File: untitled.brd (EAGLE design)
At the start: 41.6 x 28.6 mm, 21 parts, among them IC1 ACS758LCB-050B-PFF-T

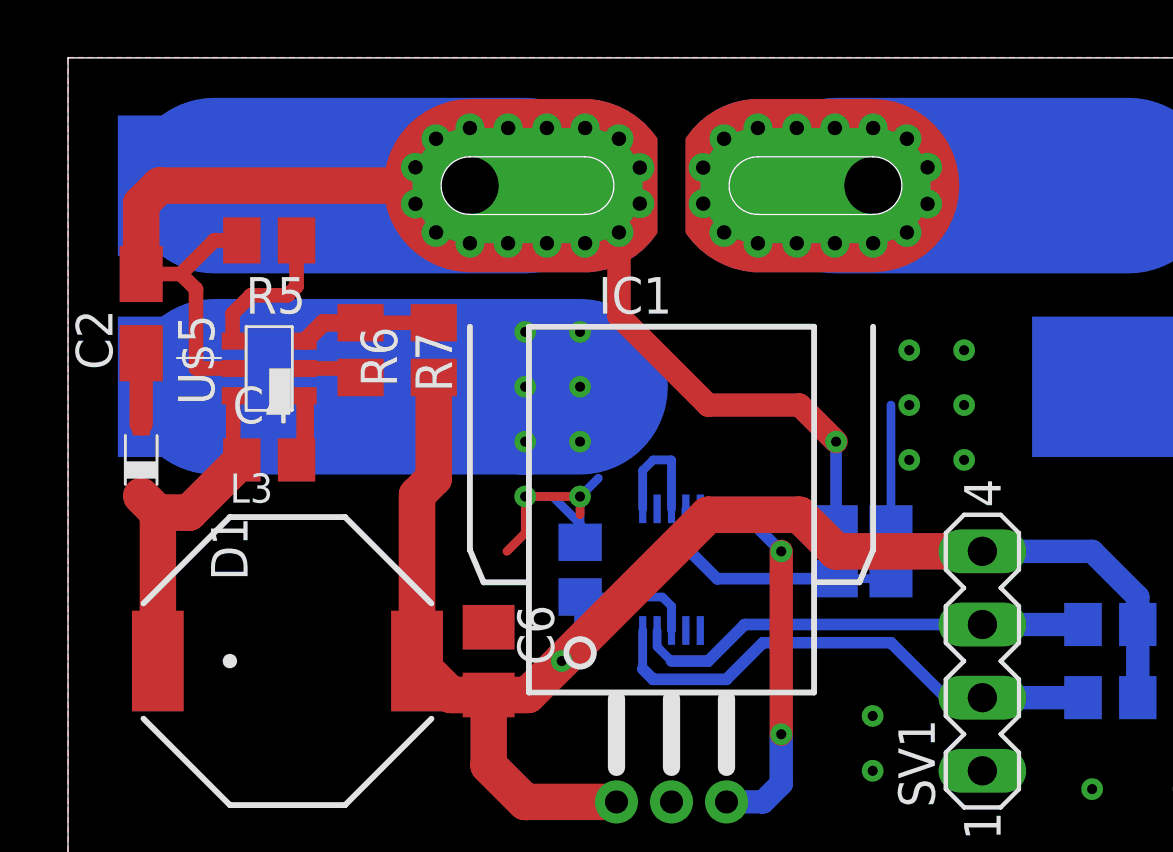
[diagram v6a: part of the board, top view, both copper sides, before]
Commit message: Update board layout based on bought components
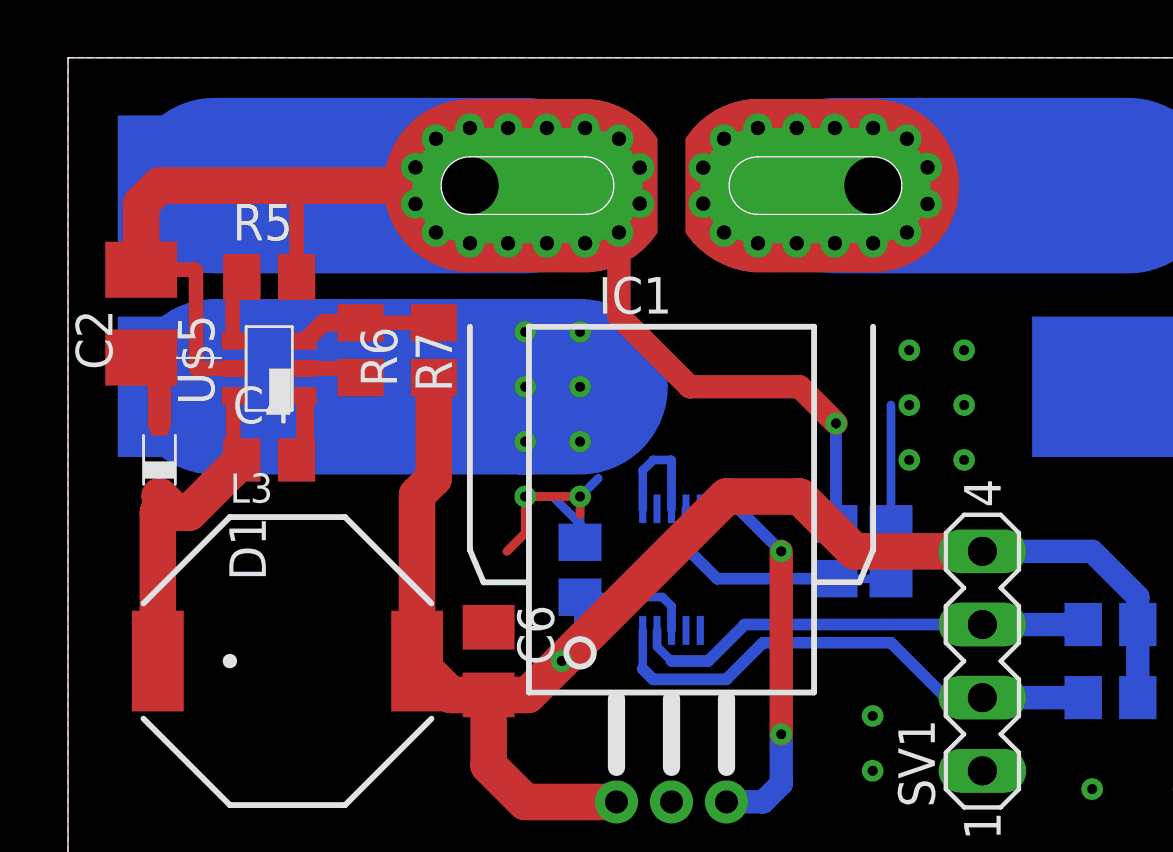
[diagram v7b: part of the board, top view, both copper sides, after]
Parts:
- C2: device rcl:A/3216-18R -> rcl:B/3528-21R
- moved R5 1.27 mm to (23.5, 36.2), turned to 0 degrees
- moved D1 0.63 mm to (19.7, 29.8)
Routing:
- net N$3: track 5.19 -> 2.55 mm
- net N$4: track 56.7 -> 58.1 mm
- net VCC: track 57.2 -> 57.7 mm
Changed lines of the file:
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@@
 <drawing>
 <settings>
-<setting alwaysvectorfont="yes"/>
+<setting alwaysvectorfont="no"/>
 <setting verticaltext="up"/>
 </settings>
@@
 <layer number="40" name="bKeepout" color="1" fill="11" visible="no" active="yes"/>
 <layer number="41" name="tRestrict" color="4" fill="10" visible="no" active="yes"/>
-<layer number="42" name="bRestrict" color="1" fill="10" visible="yes" active="yes"/>
+<layer number="42" name="bRestrict" color="1" fill="10" visible="no" active="yes"/>
 <layer number="43" name="vRestrict" color="2" fill="10" visible="no" active="yes"/>
 <layer number="44" name="Drills" color="7" fill="1" visible="no" active="yes"/>
-<layer number="45" name="Holes" color="7" fill="1" visible="yes" active="yes"/>
+<layer number="45" name="Holes" color="7" fill="1" visible="no" active="yes"/>
 <layer number="46" name="Milling" color="3" fill="1" visible="no" active="yes"/>
 <layer number="47" name="Measures" color="7" fill="1" visible="no" active="yes"/>
@@
 <attribute name="VALUE" x="22.225" y="27.305" size="1.27" layer="27"/>
 </element>
-<element name="R5" library="rcl" library_urn="urn:adsk.eagle:library:334" package="M0805" package3d_urn="urn:adsk.eagle:package:23556/2" value="100k" x="23.495" y="37.465" smashed="yes" rot="R180">
-<attribute name="NAME" x="24.765" y="36.195" size="1.27" layer="25" rot="R180"/>
-<attribute name="POPULARITY" value="45" x="23.495" y="37.465" size="1.778" layer="27" rot="R180" display="off"/>
-<attribute name="SPICEPREFIX" value="R" x="23.495" y="37.465" size="1.778" layer="27" rot="R180" display="off"/>
-<attribute name="VALUE" x="24.765" y="40.005" size="1.27" layer="27" rot="R180"/>
+<element name="R5" library="rcl" library_urn="urn:adsk.eagle:library:334" package="M0805" package3d_urn="urn:adsk.eagle:package:23556/2" value="100k" x="23.495" y="36.195" smashed="yes">
+<attribute name="NAME" x="22.225" y="37.465" size="1.27" layer="25"/>
+<attribute name="POPULARITY" value="45" x="23.495" y="36.195" size="1.778" layer="27" display="off"/>
+<attribute name="SPICEPREFIX" value="R" x="23.495" y="36.195" size="1.778" layer="27" display="off"/>
+<attribute name="VALUE" x="22.225" y="33.655" size="1.27" layer="27"/>
 </element>
 <element name="R6" library="rcl" library_urn="urn:adsk.eagle:library:334" package="M0805" package3d_urn="urn:adsk.eagle:package:23556/2" value="33k1" x="29.21" y="33.655" smashed="yes" rot="R90">
@@
 <attribute name="VALUE" x="24.13" y="34.925" size="1.27" layer="27" rot="R270"/>
 </element>
-<element name="D1" library="diode" library_urn="urn:adsk.eagle:library:210" package="SOD323_ST" package3d_urn="urn:adsk.eagle:package:43461/1" value="MBRS1100T3G" x="19.05" y="29.845" smashed="yes" rot="R90">
-<attribute name="NAME" x="22.745" y="25.655" size="1.27" layer="25" rot="R90"/>
-<attribute name="POPULARITY" value="7" x="19.05" y="29.845" size="1.778" layer="27" rot="R90" display="off"/>
-<attribute name="VALUE" x="21.05" y="28.195" size="1.27" layer="27" rot="R90"/>
-</element>
-<element name="C2" library="rcl" library_urn="urn:adsk.eagle:library:334" package="A/3216-18R" package3d_urn="urn:adsk.eagle:package:23410/2" value="2.2uF 100V" x="19.05" y="34.925" smashed="yes" rot="R90">
+<element name="D1" library="diode" library_urn="urn:adsk.eagle:library:210" package="SOD323_ST" package3d_urn="urn:adsk.eagle:package:43461/1" value="MBRS1100T3G" x="19.685" y="29.845" smashed="yes" rot="R90">
+<attribute name="NAME" x="23.38" y="25.655" size="1.27" layer="25" rot="R90"/>
+<attribute name="POPULARITY" value="7" x="19.685" y="29.845" size="1.778" layer="27" rot="R90" display="off"/>
+<attribute name="VALUE" x="21.685" y="28.195" size="1.27" layer="27" rot="R90"/>
+</element>
+<element name="C2" library="rcl" library_urn="urn:adsk.eagle:library:334" package="B/3528-21R" package3d_urn="urn:adsk.eagle:package:23409/2" value="2.2uF 100V" x="19.05" y="34.925" smashed="yes" rot="R90">
 <attribute name="NAME" x="18.05" y="32.975" size="1.27" layer="25" rot="R90"/>
 <attribute name="POPULARITY" value="1" x="19.05" y="34.925" size="1.778" layer="27" rot="R90" display="off"/>
@@
 <contactref element="C2" pad="-"/>
 <contactref element="C6" pad="-"/>
-<wire x1="19.05" y1="33.55" x2="19.05" y2="31.095" width="0.8128" layer="1"/>
+<wire x1="19.05" y1="33.4" x2="19.685" y2="32.915" width="0.8128" layer="1"/>
+<wire x1="19.685" y1="32.915" x2="19.685" y2="31.095" width="0.8128" layer="1"/>
 <wire x1="24.745" y1="33.02" x2="26.355" y2="33.02" width="0.508" layer="1"/>
 <wire x1="26.355" y1="33.02" x2="26.67" y2="32.705" width="0.508" layer="1"/>
-<polygon width="0.508" layer="1" isolate="0.3048">
+<polygon width="0.508" layer="1" isolate="0.4064">
 <vertex x="16.51" y="43.815"/>
 <vertex x="57.785" y="43.815"/>
@@
 <wire x1="33.655" y1="22.86" x2="32.48" y2="21.685" width="1.27" layer="1"/>
 <wire x1="32.48" y1="21.685" x2="31.115" y2="21.685" width="1.27" layer="1"/>
-<wire x1="48.26" y1="26.67" x2="43.18" y2="26.67" width="1.27" layer="1"/>
-<wire x1="43.18" y1="26.67" x2="41.91" y2="27.94" width="1.27" layer="1"/>
-<wire x1="41.91" y1="27.94" x2="38.735" y2="27.94" width="1.27" layer="1"/>
-<wire x1="38.735" y1="27.94" x2="33.655" y2="22.86" width="1.27" layer="1"/>
+<wire x1="48.26" y1="26.67" x2="43.815" y2="26.67" width="1.27" layer="1"/>
+<wire x1="43.815" y1="26.67" x2="41.91" y2="28.575" width="1.27" layer="1"/>
+<wire x1="41.91" y1="28.575" x2="39.37" y2="28.575" width="1.27" layer="1"/>
+<wire x1="39.37" y1="28.575" x2="33.655" y2="22.86" width="1.27" layer="1"/>
 </signal>
 <signal name="N$13">
@@
 <wire x1="21.59" y1="39.37" x2="32.385" y2="39.37" width="6.096" layer="16"/>
 <wire x1="35.64" y1="37.745" x2="35.64" y2="34.845" width="0.8128" layer="1"/>
-<wire x1="35.64" y1="34.845" x2="38.735" y2="31.75" width="0.8128" layer="1"/>
-<wire x1="30.465" y1="39.37" x2="19.685" y2="39.37" width="1.27" layer="1"/>
+<wire x1="35.64" y1="34.845" x2="38.1" y2="32.385" width="0.8128" layer="1"/>
+<wire x1="30.465" y1="39.37" x2="24.765" y2="39.37" width="1.27" layer="1"/>
+<wire x1="24.765" y1="39.37" x2="19.685" y2="39.37" width="1.27" layer="1"/>
 <wire x1="19.685" y1="39.37" x2="19.05" y2="38.735" width="1.27" layer="1"/>
-<wire x1="19.05" y1="38.735" x2="19.05" y2="36.3" width="1.27" layer="1"/>
+<wire x1="19.05" y1="38.735" x2="19.05" y2="36.45" width="1.27" layer="1"/>
 <wire x1="22.245" y1="33.02" x2="20.955" y2="33.02" width="0.508" layer="1"/>
-<wire x1="22.545" y1="37.465" x2="21.59" y2="37.465" width="0.508" layer="1"/>
-<wire x1="20.425" y1="36.3" x2="19.05" y2="36.3" width="0.508" layer="1"/>
-<wire x1="21.59" y1="37.465" x2="20.425" y2="36.3" width="0.508" layer="1"/>
-<wire x1="20.955" y1="35.77" x2="20.425" y2="36.3" width="0.508" layer="1"/>
-<wire x1="20.955" y1="33.02" x2="20.955" y2="35.77" width="0.508" layer="1"/>
-<via x="43.18" y="30.48" extent="1-16" drill="0.35"/>
-<wire x1="43.18" y1="30.48" x2="41.91" y2="31.75" width="0.8128" layer="1"/>
-<wire x1="41.91" y1="31.75" x2="38.735" y2="31.75" width="0.8128" layer="1"/>
-<wire x1="43.18" y1="27.62" x2="43.18" y2="30.48" width="0.4064" layer="16"/>
+<wire x1="20.91" y1="36.45" x2="19.05" y2="36.45" width="0.508" layer="1"/>
+<wire x1="20.955" y1="36.405" x2="20.91" y2="36.45" width="0.508" layer="1"/>
+<wire x1="20.955" y1="33.02" x2="20.955" y2="36.405" width="0.508" layer="1"/>
+<via x="43.18" y="31.115" extent="1-16" drill="0.35"/>
+<wire x1="43.18" y1="31.115" x2="41.91" y2="32.385" width="0.8128" layer="1"/>
+<wire x1="41.91" y1="32.385" x2="38.1" y2="32.385" width="0.8128" layer="1"/>
+<wire x1="43.18" y1="27.62" x2="43.18" y2="31.115" width="0.4064" layer="16"/>
+<wire x1="24.445" y1="36.195" x2="24.445" y2="39.05" width="0.508" layer="1"/>
+<wire x1="24.445" y1="39.05" x2="24.765" y2="39.37" width="0.508" layer="1"/>
 <wire x1="33.655" y1="38.735" x2="33.02" y2="38.735" width="0" layer="19" extent="1-16"/>
 </signal>
@@
 <contactref element="U$5" pad="4"/>
 <contactref element="R5" pad="1"/>
-<wire x1="24.445" y1="37.44" x2="24.445" y2="37.465" width="0.508" layer="1"/>
 <wire x1="22.245" y1="33.97" x2="22.225" y2="33.99" width="0.508" layer="1"/>
-<wire x1="22.225" y1="33.99" x2="22.225" y2="34.925" width="0.508" layer="1"/>
-<wire x1="22.225" y1="34.925" x2="22.86" y2="35.56" width="0.508" layer="1"/>
-<wire x1="22.86" y1="35.56" x2="24.13" y2="35.56" width="0.508" layer="1"/>
-<wire x1="24.13" y1="35.56" x2="24.445" y2="35.875" width="0.508" layer="1"/>
-<wire x1="24.445" y1="35.875" x2="24.445" y2="37.465" width="0.508" layer="1"/>
+<wire x1="22.225" y1="36.195" x2="22.225" y2="33.99" width="0.508" layer="1"/>
+<wire x1="22.545" y1="36.195" x2="22.225" y2="36.195" width="0.508" layer="1"/>
 </signal>
 <signal name="N$9">
@@
 <wire x1="22.545" y1="29.845" x2="22.245" y2="30.145" width="0.508" layer="1"/>
 <wire x1="22.245" y1="30.145" x2="22.245" y2="32.07" width="0.508" layer="1"/>
-<wire x1="19.05" y1="28.595" x2="19.63" y2="28.015" width="1.27" layer="1"/>
+<wire x1="19.685" y1="28.595" x2="20.265" y2="28.015" width="1.27" layer="1"/>
 <wire x1="19.63" y1="28.015" x2="19.63" y2="22.86" width="1.27" layer="1"/>
 <wire x1="22.545" y1="29.845" x2="20.715" y2="28.015" width="1.27" layer="1"/>
-<wire x1="20.715" y1="28.015" x2="19.63" y2="28.015" width="1.27" layer="1"/>
+<wire x1="20.715" y1="28.015" x2="20.265" y2="28.015" width="1.27" layer="1"/>
+<wire x1="20.265" y1="28.015" x2="19.63" y2="28.015" width="1.27" layer="1"/>
 </signal>
 <signal name="N$10">

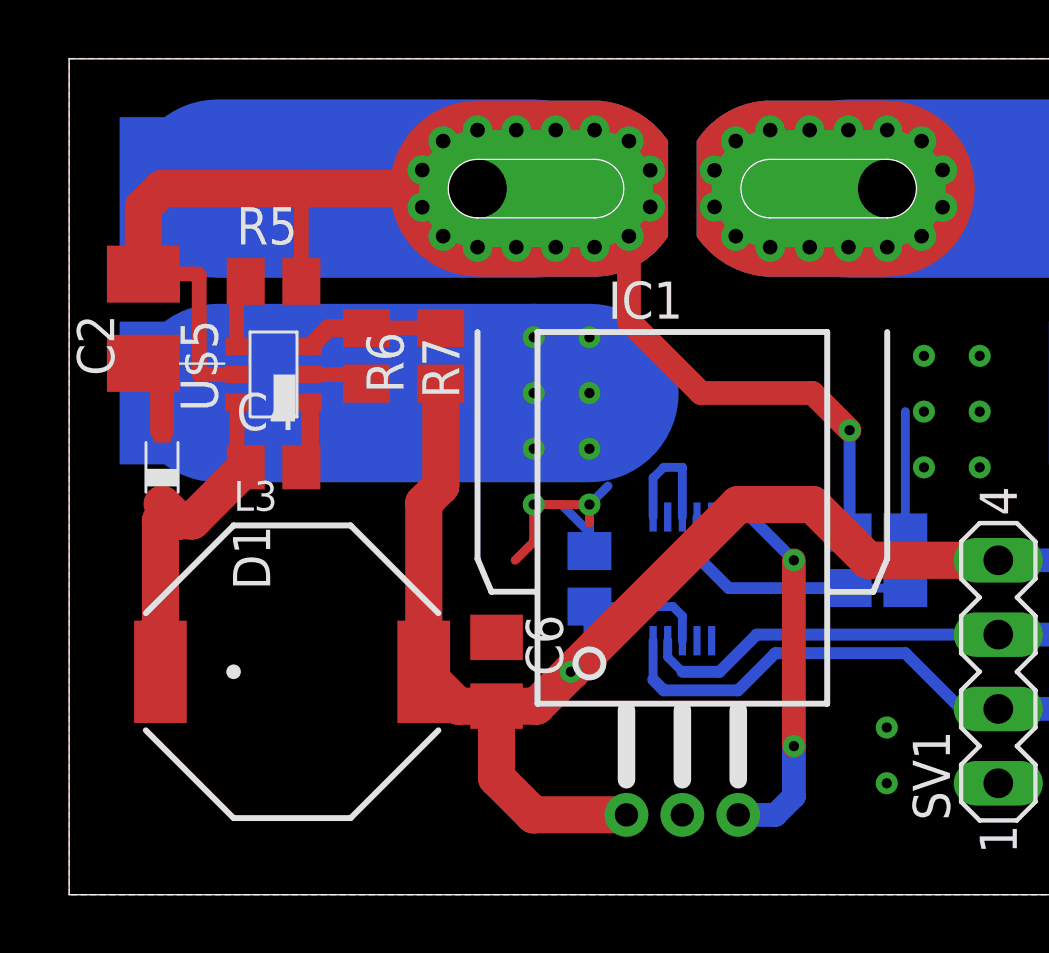
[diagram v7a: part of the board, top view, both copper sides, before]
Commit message: Another PCB updated to match new components
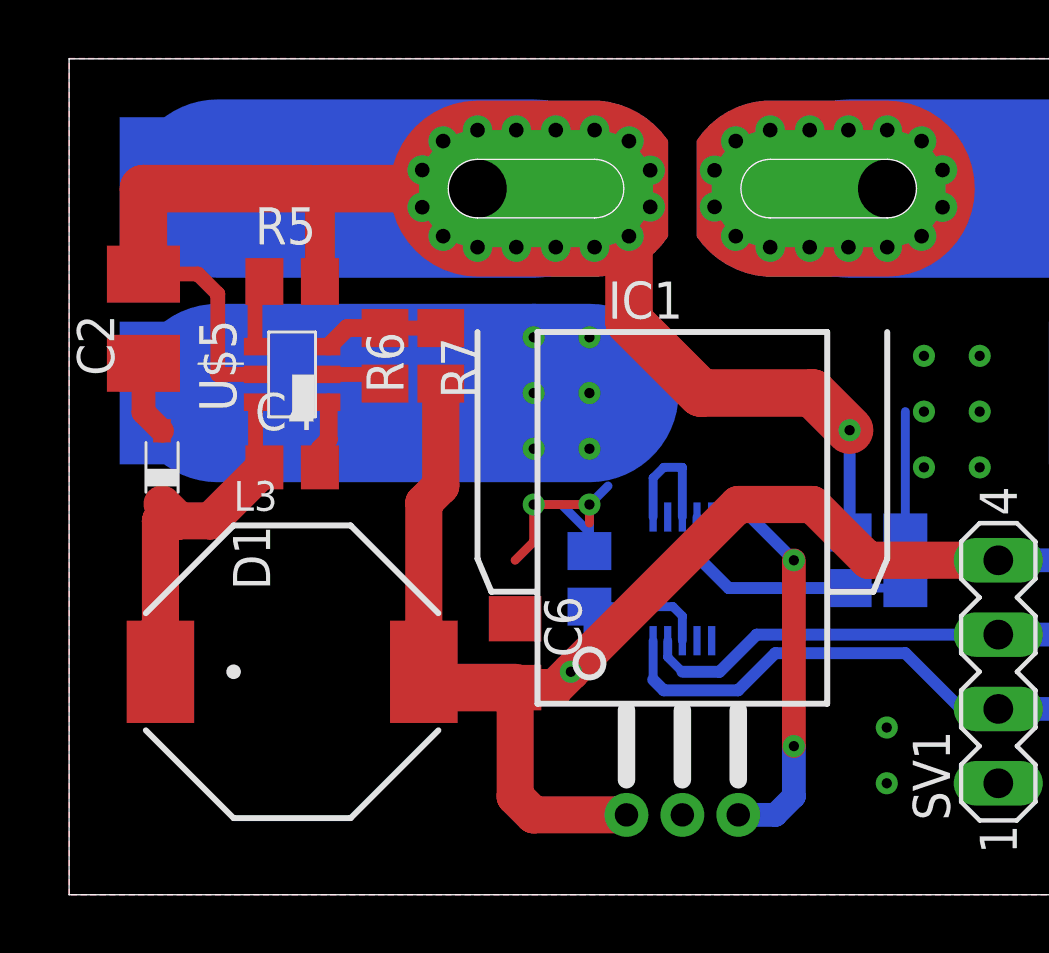
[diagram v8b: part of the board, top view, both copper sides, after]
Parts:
- moved C6 0.90 mm to (31.8, 23.5)
- moved C4 0.63 mm to (24.1, 29.8)
- moved R5 0.63 mm to (24.1, 36.2)
- moved R7 0.63 mm to (27.3, 33.7)
- moved U$5 0.63 mm to (24.1, 33.0)
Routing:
- net N$11: track 4.73 -> 4.09 mm
- net N$9: track 12.0 -> 12.6 mm
